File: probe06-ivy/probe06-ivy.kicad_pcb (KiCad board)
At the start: 2 copper layers, 81 x 81 mm, 108 parts, among them J1 USB_B_Micro, J2 Conn_Coaxial, Q1 S9014, SW1 SW_Push, SW2 SW_SPDT, U1 STM32F407VGTx, U2 MP1584EN, U3 AMS1117-3.3, U6 24LC32, Y1 8 MHz, Y2 32.768 KHz

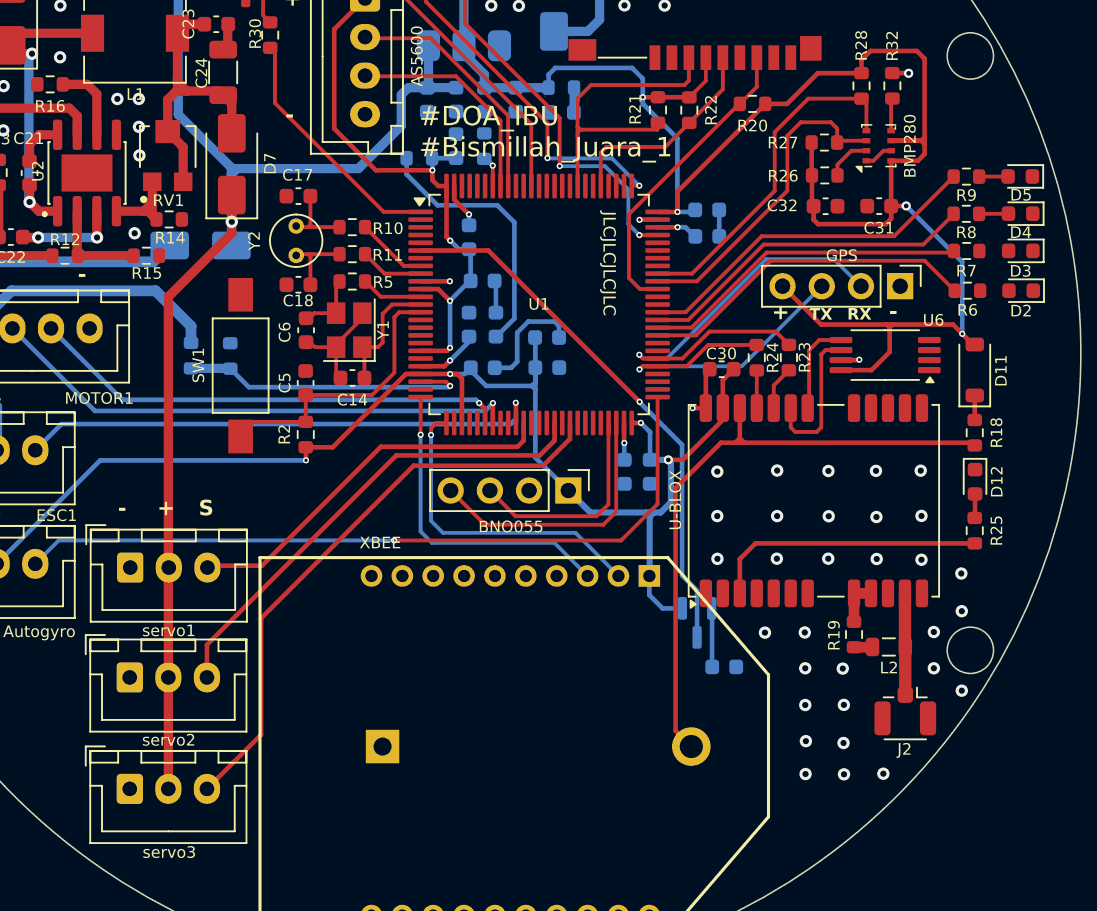
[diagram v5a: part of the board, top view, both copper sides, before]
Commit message: Some revision to meet pcb service requirements - Change via hole diameter - Via and component placement - etc
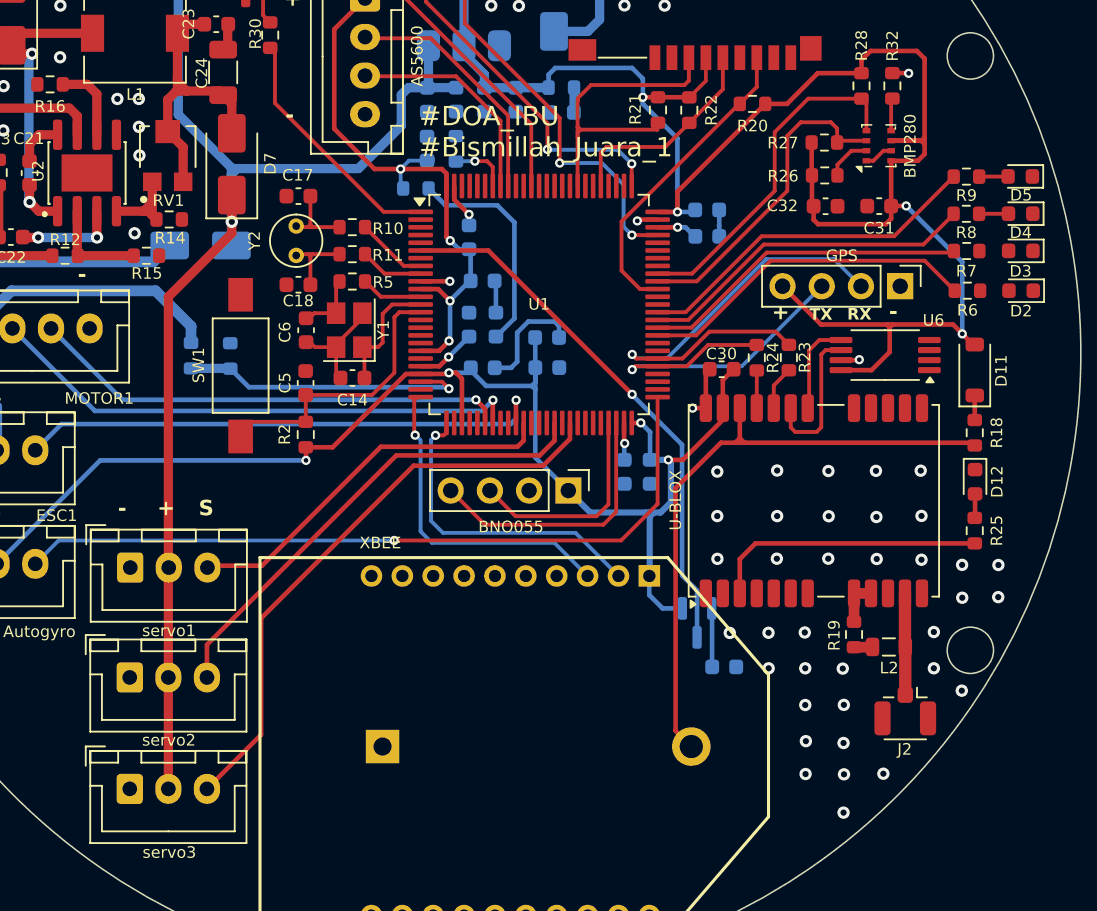
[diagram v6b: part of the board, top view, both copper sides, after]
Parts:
- moved R1 1.97 mm to (143.5, 92.7), turned to 0 degrees
- moved C7 1.89 mm to (144.3, 90.1)
- moved R3 1.85 mm to (146.1, 90.1)
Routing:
- net /VREF+: track 21.3 -> 18.3 mm
- net Net-(U1-BOOT0): track 2.05 -> 3.79 mm
- net +3V3: track 252.8 -> 253.9 mm
- net TX3: track 22.3 -> 23.3 mm
- net RX3: track 28.7 -> 29.7 mm
- net GND: track 33.5 -> 33.6 mm, vias 59 -> 64
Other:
- board text added: "Garudaku Jaya Di Angkasa"
- board text removed: "Garudaku Jaya Diangkasa"
- board text removed: "JLCJLCJLCJLC"

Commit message: rev 1.2
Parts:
- removed the D10 at (135.0, 68.1)
- removed D11: D, Diode_SMD:D_SOD-123
- removed the R18 at (179.7, 108.5)
- removed SW2: SW_SPDT, Button_Switch_THT:SW_Slide_SPDT_Angled_CK_OS102011MA1Q
- added LED_PWR1: xx, Connector_JST:JST_XH_B2B-XH-A_1x02_P2.50mm_Vertical, F.Cu at (181.2, 107.2)
- added PWR_SW1: xx, Connector_JST:JST_XH_B2B-XH-A_1x02_P2.50mm_Vertical, F.Cu at (109.9, 100.6)
- D9, R17: moved to F.Cu
- SD1: renamed from SD CARD
- U4: renamed from U-BLOX; value U-BLOX -> NEO-M8M
- moved R17 53.3 mm to (182.7, 110.9), turned to 0 degrees
- moved D8 29.6 mm to (127.8, 96.8), turned to 0 degrees
- moved D9 18.0 mm to (111.6, 95.2)
- moved BATT1 13.4 mm to (108.7, 108.4), turned to 0 degrees
- moved R29 5.87 mm to (135.1, 88.5)
- moved Q1 5.68 mm to (134.5, 84.6)
- moved C20 3.17 mm to (112.2, 90.8), turned to 180 degrees
- moved C19 2.81 mm to (116.9, 86.6), turned to 90 degrees
- moved MOTOR1 1.98 mm to (116.8, 102.1)
- moved R15 1.12 mm to (125.1, 97.5)
- moved R12 0.52 mm to (120.8, 97.5)
- renumbered AS5600 to AS5600_Encoder1, Autogyro to Autogyro1, BNO055 to BNO1, D12 to D10, GPS to GPS1, R19 to R18, R20 to R19, R21 to R20, R22 to R21, R23 to R22, R24 to R23, R25 to R24, R26 to R25, R27 to R26, R28 to R27, R29 to R28, R30 to R29, R31 to R30, R32 to R31, SWD to SWD1, XBEE to U5, BMP280 to U7
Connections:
- BATT1 pad 1: +BATT -> Net-(BATT1-Pin_1)
- C26 pad 1: +5V -> +BATT
- C27 pad 1: +5V -> +BATT
- D8 pad 1: +5V -> +BATT
- D8 pad 2: +U5V -> +5V
- D9 pad 1: +5V -> +BATT
- J1 pad 1: +U5V -> +5V
- SWD1 pad 1: +U5V -> +5V
- U3 pad 3: +5V -> +BATT
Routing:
- net +5V: track 126.3 -> 97.3 mm
- net GND: track 33.6 -> 58.6 mm, vias 64 -> 67
- net +BATT: track 72.1 -> 93.3 mm
- net Net-(D9-A): track 21.5 -> 5.55 mm
- net +U5V: track 13.0 -> 0.00 mm
- net +3V3: track 253.9 -> 265.3 mm
- net +3V0: track 44.4 -> 33.1 mm
- net Autogyro: track 48.8 -> 56.5 mm, vias 1 -> 0
- net Net-(LED_PWR1-Pin_1): track 11.7 -> 4.64 mm, vias 1 -> 0
- net Net-(CAM1-Pin_1): track 6.26 -> 12.8 mm
- net Net-(CAM1-Pin_2): track 4.40 -> 10.5 mm
- net Net-(BATT1-Pin_1): track 0.00 -> 5.75 mm
- net CAM: track 16.1 -> 10.8 mm
- net PWM2: track 35.1 -> 33.0 mm
- net PWM1: track 31.2 -> 29.1 mm
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
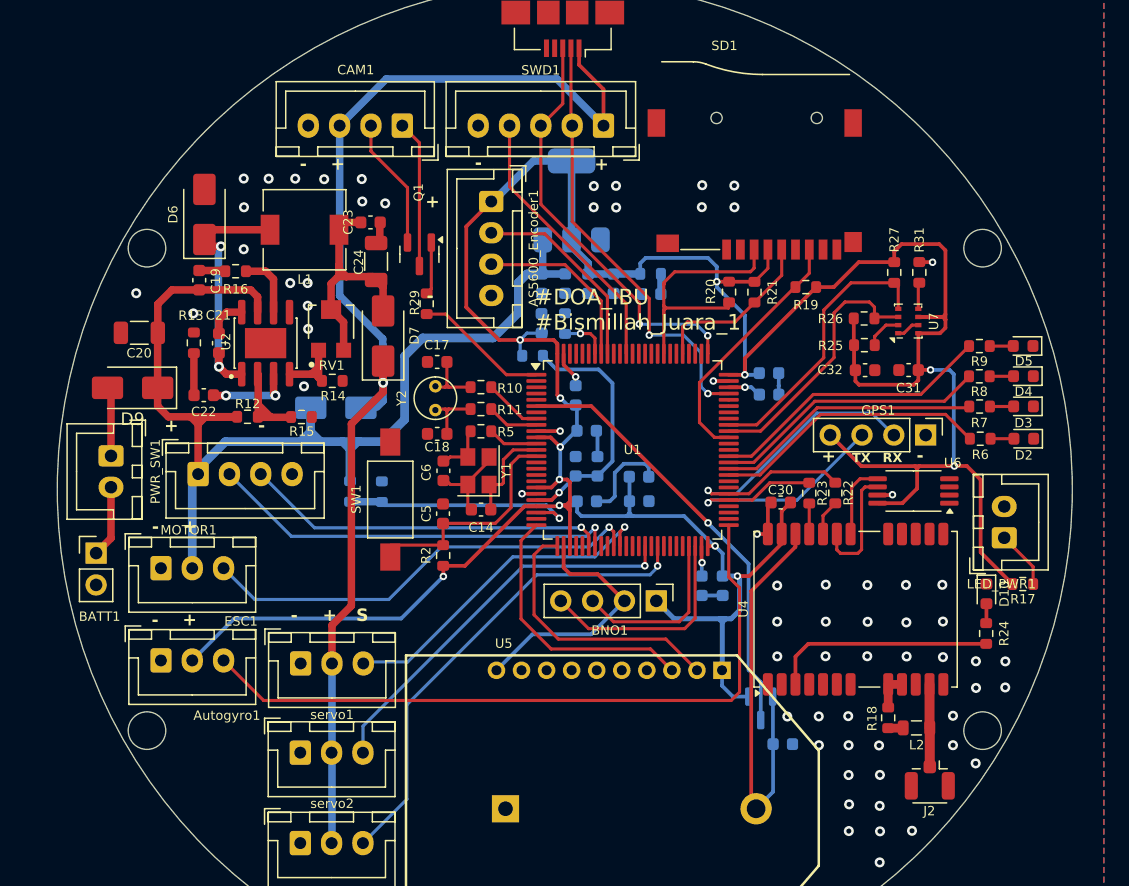
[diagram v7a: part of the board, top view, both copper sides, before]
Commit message: rev 1.2.1 add additional pin
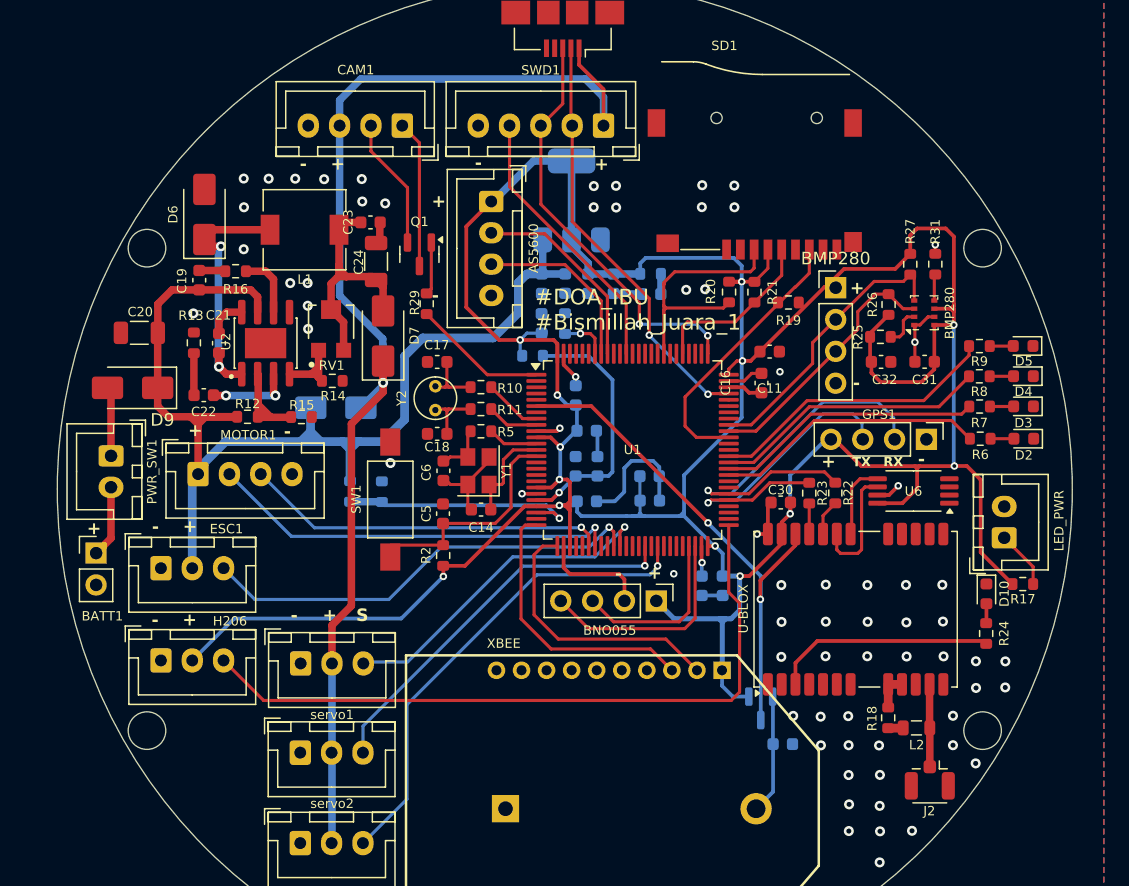
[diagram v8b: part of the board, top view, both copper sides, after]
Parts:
- added BMP280: xx, Connector_PinHeader_2.54mm:PinHeader_1x04_P2.54mm_Vertical, F.Cu at (167.7, 87.2)
- added G***: LOGO, Images:roki2, B.Cu at (171.3, 82.8)
- C11, C16: moved to F.Cu
- moved G*** 3.94 mm to (160.2, 82.1)
- moved R26 2.25 mm to (171.9, 88.6), turned to 90 degrees
- moved R19 1.85 mm to (164.0, 88.4)
- moved C11 1.72 mm to (162.5, 92.3)
- moved BMP280 1.44 mm to (174.8, 89.2)
- moved C32 1.44 mm to (171.4, 93.1)
- moved R25 1.44 mm to (171.3, 91.1)
- moved R27 1.44 mm to (173.7, 85.3)
- moved R31 1.44 mm to (175.7, 85.3)
- moved C31 1.44 mm to (174.8, 93.1)
- moved C16 1.10 mm to (161.8, 94.8), turned to 90 degrees
- moved C10 0.85 mm to (152.9, 102.3)
- moved C4 0.85 mm to (152.9, 104.2)
- moved GPS1 0.35 mm to (175.0, 99.3)
- renumbered AS5600_Encoder1 to AS5600, U7 to BMP280, BNO1 to BNO055, Autogyro1 to H206, LED_PWR1 to LED_PWR, U4 to U-BLOX, U5 to XBEE
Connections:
- D1 pad 3: /VBAT -> VBAT
- U-BLOX pad 22: +3V0 -> VBAT
- U1 pad 6: /VBAT -> VBAT
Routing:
- net VBAT: track 0.00 -> 41.4 mm, vias 0 -> 2
- net /VBAT: track 35.0 -> 0.00 mm, vias 1 -> 0
- net +3V0: track 33.1 -> 9.53 mm
- net +3V3: track 265.3 -> 287.1 mm, vias 12 -> 13
- net +5V: track 97.3 -> 100.4 mm
- net GND: track 58.6 -> 55.7 mm, vias 67 -> 70
- net TX3: track 23.3 -> 25.7 mm
- net SDIO_D0: track 20.3 -> 22.1 mm
- net SWDIO: track 35.8 -> 34.3 mm
- net RX3: track 29.7 -> 31.2 mm
- net /VREF+: track 20.1 -> 20.7 mm
- net SDA3: track 21.0 -> 20.4 mm
- net TX2: track 21.7 -> 22.2 mm
- net Net-(U1-VCAP_2): track 2.64 -> 2.80 mm, vias 1 -> 0
